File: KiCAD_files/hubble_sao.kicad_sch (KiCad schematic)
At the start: 43 parts, among them J1 Conn_02x03_Counter_Clockwise, J2 Conn_02x03_Odd_Even, Q1 DMP3099L-7, SW1 SW_Push_Shielded, SW2 SW_Push, U1 VEML3328, U2 LSM6DSO, U3 ATmega328PB-A, U4 TLV9062xD, U5 TLV9062xD

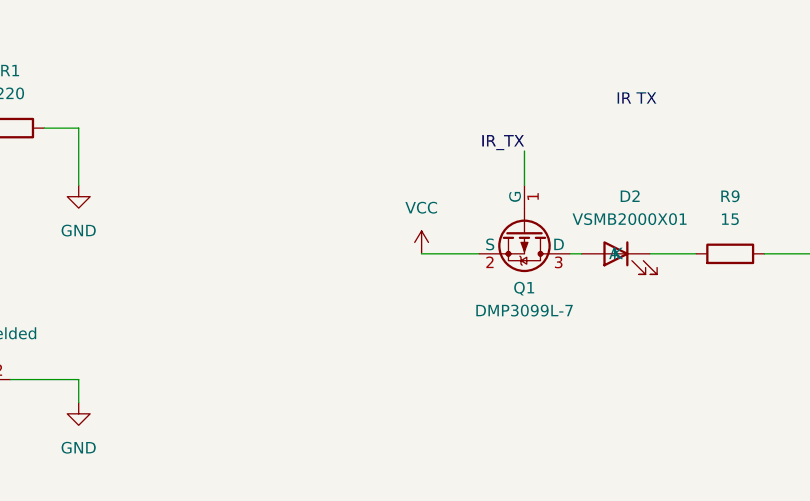
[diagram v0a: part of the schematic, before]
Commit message: Added decoupling cap for the IR_TX LED (DNP for now) and touched up some tracks around there
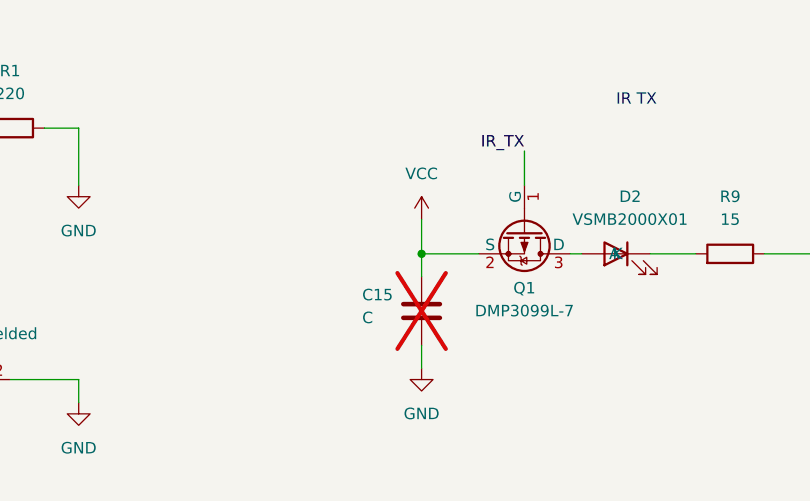
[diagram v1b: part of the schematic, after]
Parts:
- added C15: C, Capacitor_SMD:C_0603_1608Metric_Pad1.08x0.95mm_HandSolder, symbol Device:C
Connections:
- net GND: now also C15.2
- net VCC: now also C15.1
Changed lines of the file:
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@@
 	)
 	(junction
+		(at 88.9 165.1)
+		(diameter 0)
+		(color 0 0 0 0)
+	)
+	(junction
 		(at 167.64 100.33)
 		(diameter 0)
@@
 	(wire
 		(pts
+			(xy 88.9 161.29) (xy 88.9 165.1)
+		)
+		(stroke
+			(width 0)
+			(type default)
+		)
+	)
+	(wire
+		(pts
 			(xy 152.4 132.08) (xy 167.64 132.08)
 		)
@@
 	(wire
 		(pts
+			(xy 88.9 165.1) (xy 88.9 167.64)
+		)
+		(stroke
+			(width 0)
+			(type default)
+		)
+	)
+	(wire
+		(pts
 			(xy 228.6 133.35) (xy 228.6 132.08)
 		)
@@
 	(wire
 		(pts
+			(xy 88.9 175.26) (xy 88.9 177.8)
+		)
+		(stroke
+			(width 0)
+			(type default)
+		)
+	)
+	(wire
+		(pts
 			(xy 104.14 58.42) (xy 104.14 60.96)
 		)
@@
 	)
 	(symbol
+		(lib_id "Device:C")
+		(at 88.9 171.45 0)
+		(unit 1)
+		(exclude_from_sim no)
+		(in_bom yes)
+		(on_board yes)
+		(dnp yes)
+		(property "Reference" "C15"
+			(at 82.296 169.672 0)
+			(effects
+				(font
+					(size 1.27 1.27)
+				)
+				(justify left)
+			)
+		)
+		(property "Value" "C"
+			(at 82.296 172.212 0)
+			(effects
+				(font
+					(size 1.27 1.27)
+				)
+				(justify left)
+			)
+		)
+		(property "Footprint" "Capacitor_SMD:C_0603_1608Metric_Pad1.08x0.95mm_HandSolder"
+			(at 89.8652 175.26 0)
+			(effects
+				(font
+					(size 1.27 1.27)
+				)
+				(hide yes)
+			)
+		)
+		(property "Datasheet" "~"
+			(at 88.9 171.45 0)
+			(effects
+				(font
+					(size 1.27 1.27)
+				)
+				(hide yes)
+			)
+		)
+		(property "Description" "Unpolarized capacitor"
+			(at 88.9 171.45 0)
+			(effects
+				(font
+					(size 1.27 1.27)
+				)
+				(hide yes)
+			)
+		)
+		(pin "2"
+		)
+		(pin "1"
+		)
+		(instances
+			(project ""
+				(path "/9cd05651-fad9-4e28-8d04-6923ebe26f0c"
+					(reference "C15")
+					(unit 1)
+				)
+			)
+		)
+	)
+	(symbol
 		(lib_id "Device:R_Small")
 		(at 266.7 39.37 0)
@@
 	(symbol
 		(lib_id "power:GND")
+		(at 88.9 177.8 0)
+		(unit 1)
+		(exclude_from_sim no)
+		(in_bom yes)
+		(on_board yes)
+		(dnp no)
+		(fields_autoplaced yes)
+		(property "Reference" "#PWR040"
+			(at 88.9 184.15 0)
+			(effects
+				(font
+					(size 1.27 1.27)
+				)
+				(hide yes)
+			)
+		)
+		(property "Value" "GND"
+			(at 88.9 182.88 0)
+			(effects
+				(font
+					(size 1.27 1.27)
+				)
+			)
+		)
+		(property "Footprint" ""
+			(at 88.9 177.8 0)
+			(effects
+				(font
+					(size 1.27 1.27)
+				)
+				(hide yes)
+			)
+		)
+		(property "Datasheet" ""
+			(at 88.9 177.8 0)
+			(effects
+				(font
+					(size 1.27 1.27)
+				)
+				(hide yes)
+			)
+		)
+		(property "Description" "Power symbol creates a global label with name \"GND\" , ground"
+			(at 88.9 177.8 0)
+			(effects
+				(font
+					(size 1.27 1.27)
+				)
+				(hide yes)
+			)
+		)
+		(pin "1"
+		)
+		(instances
+			(project ""
+				(path "/9cd05651-fad9-4e28-8d04-6923ebe26f0c"
+					(reference "#PWR040")
+					(unit 1)
+				)
+			)
+		)
+	)
+	(symbol
+		(lib_id "power:GND")
 		(at 152.4 111.76 0)
 		(unit 1)
@@
 	(symbol
 		(lib_id "power:VCC")
-		(at 88.9 165.1 0)
+		(at 88.9 161.29 0)
 		(mirror y)
 		(unit 1)
@@
 		(fields_autoplaced yes)
 		(property "Reference" "#PWR033"
-			(at 88.9 168.91 0)
+			(at 88.9 165.1 0)
 			(effects
 				(font
@@
 		)
 		(property "Value" "VCC"
-			(at 88.9 160.02 0)
+			(at 88.9 156.21 0)
 			(effects
 				(font
@@
 		)
 		(property "Footprint" ""
-			(at 88.9 165.1 0)
+			(at 88.9 161.29 0)
 			(effects
 				(font
@@
 		)
 		(property "Datasheet" ""
-			(at 88.9 165.1 0)
+			(at 88.9 161.29 0)
 			(effects
 				(font
@@
 		)
 		(property "Description" "Power symbol creates a global label with name \"VCC\""
-			(at 88.9 165.1 0)
+			(at 88.9 161.29 0)
 			(effects
 				(font

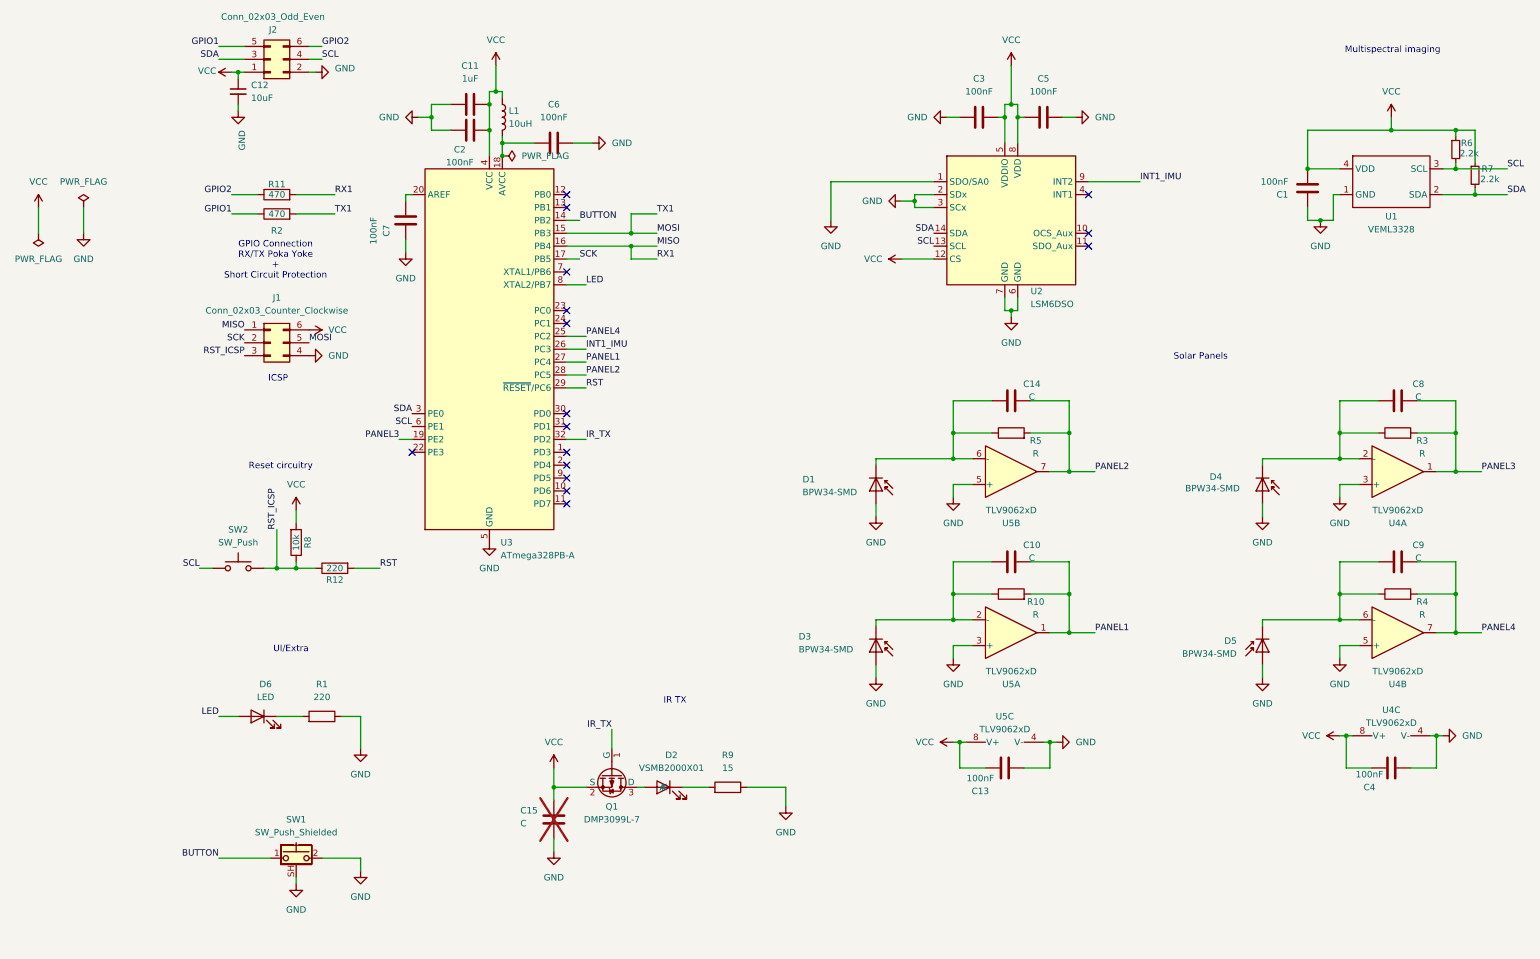
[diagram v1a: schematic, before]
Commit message: Modified blinky LEDs
- Changed reverse mount LED for a side view LED
- Added a WS2812N (Neopixel)
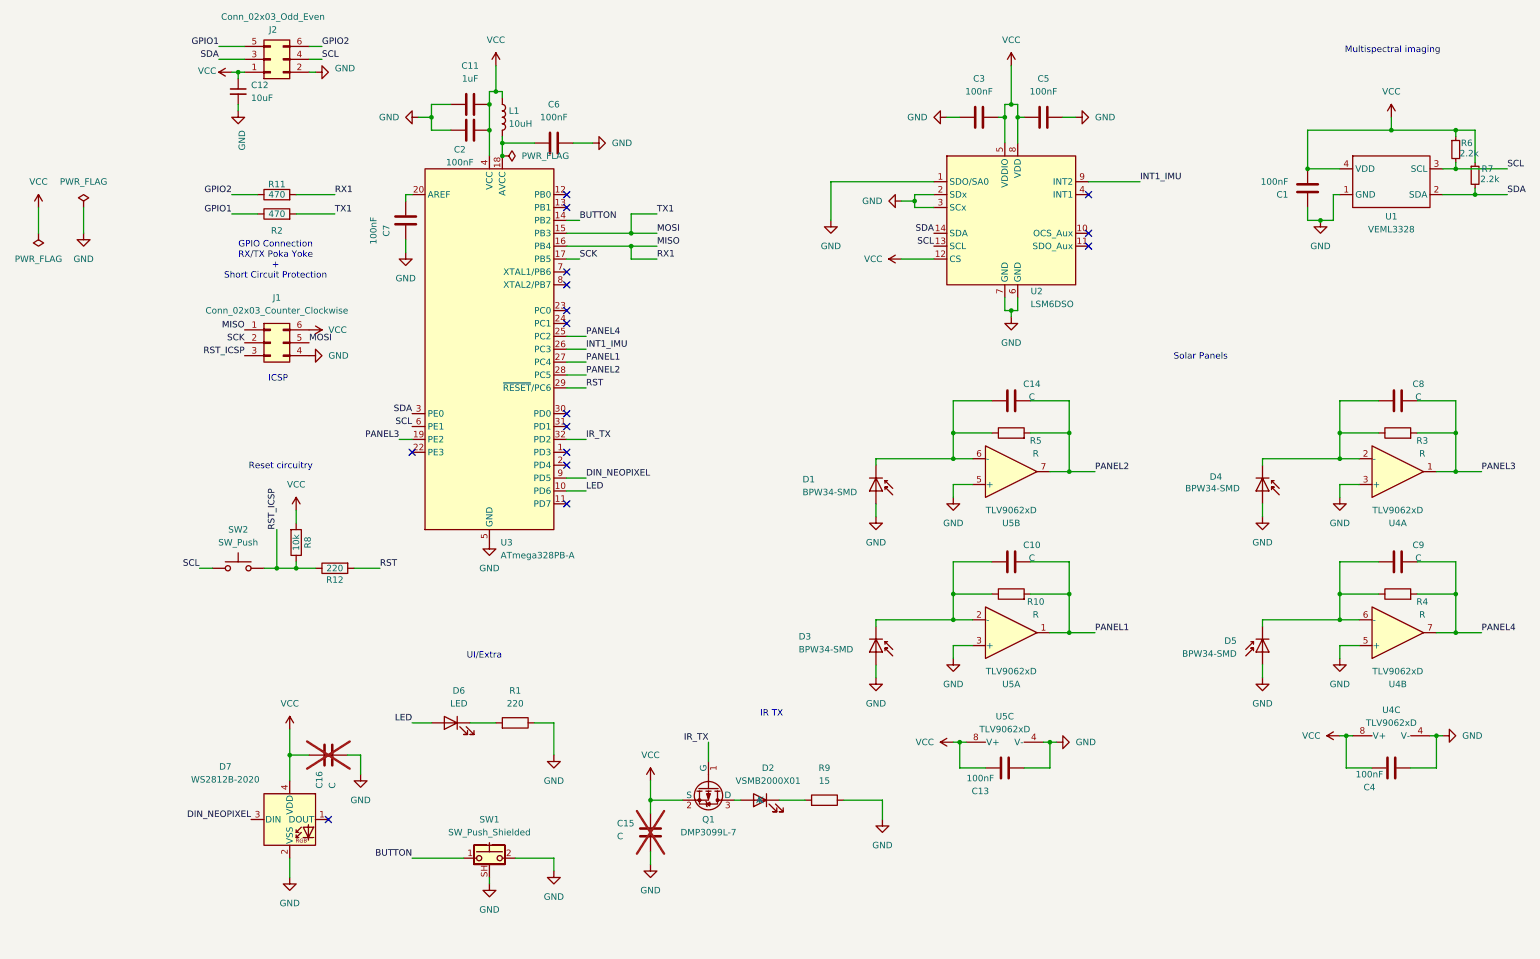
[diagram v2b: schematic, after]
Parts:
- added C16: C, Capacitor_SMD:C_0603_1608Metric_Pad1.08x0.95mm_HandSolder, symbol Device:C
- added D7: WS2812B-2020, LED_SMD:LED_WS2812B-2020_PLCC4_2.0x2.0mm, symbol LED:WS2812B-2020
- D6: footprint LED_SMD:LED_1206_3216Metric_ReverseMount_Hole1.8x2.4mm -> optical_sensors:LED_LiteOn_LTST-S110
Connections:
- net GND: now also C16.2, D7.2 (VSS)
- net LED: now also U3.10 (PD6); no longer U3.8 (XTAL2/PB7)
- net VCC: now also C16.1, D7.4 (VDD)
- net DIN_NEOPIXEL: now reaches U3.9 (PD5)
- net DIN_NEOPIXEL: now also D7.3 (DIN)
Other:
- moved on the sheet: C15, D2, D6, Q1, R1, R9, SW1

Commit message: Touched up the schematic
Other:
- note added: "ICSP pads"
- note added: "IMU (Acc + Gyro)"
- note added: "Multispectral imaging (Color sensor)"
- note added: "Neopixel (WS2818B)"
- note added: "Push button"
- note added: "SAO Connector"
- note added: "Simple LED"
- note removed: "ICSP"
- note removed: "Multispectral imaging"
- moved on the sheet: C10, C11, C12, C13, C14, C15, C2, C4, C6, C7, D1, D2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

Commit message: Updated version number to 2.0 and metadata
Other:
- company: (none) -> pdulab
- title: (none) -> Hubble SAO
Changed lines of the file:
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@@
 	(generator_version "8.0")
 	(paper "A4")
+	(title_block
+		(title "Hubble SAO")
+		(rev "2.0")
+		(company "pdulab")
+	)
 	(junction
 		(at 266.7 35.56)
